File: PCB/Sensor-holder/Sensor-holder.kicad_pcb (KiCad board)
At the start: 2 copper layers, 35.1 x 22.9 mm, 25 parts, among them P1 CONN_01X05, Q1 IRLML6402, Q2 IRLML6402, Q3 IRLML6402, U1 DRV5013AD, U2 DRV5013AD, U3 DRV5013AD

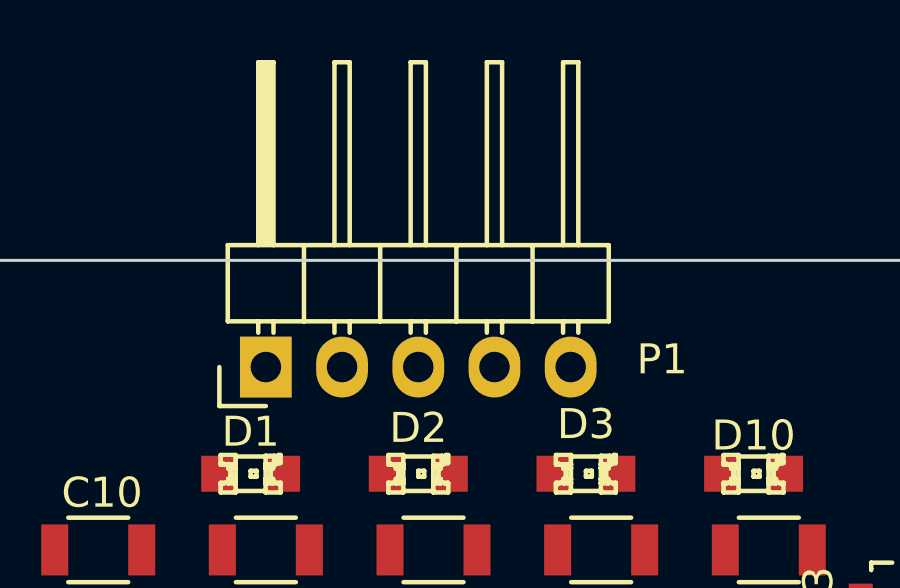
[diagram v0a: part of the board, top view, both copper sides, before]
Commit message: Design Regeln für die Leiterbahnen und Vias definiert. Einstellungen aus dem Teensy Projekt.
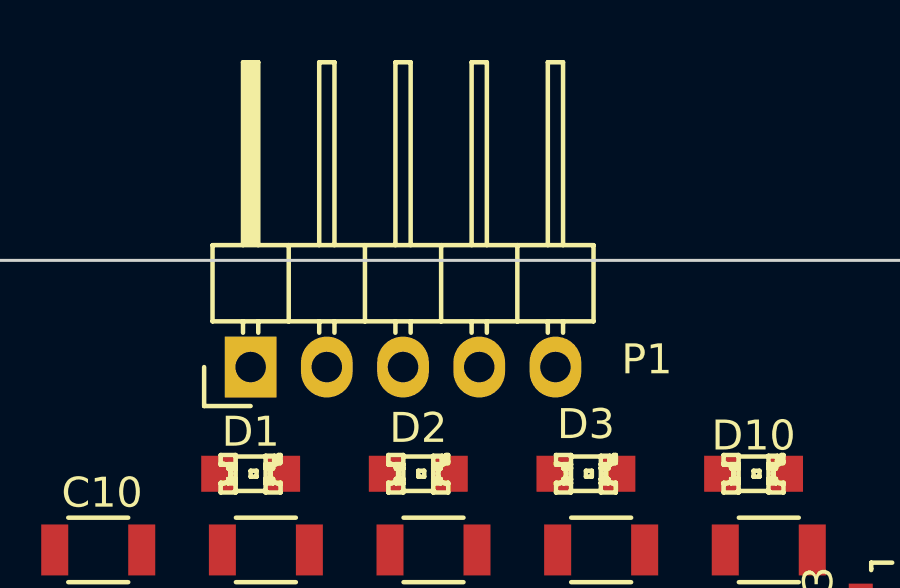
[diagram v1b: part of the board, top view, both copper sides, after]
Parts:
- moved P1 0.51 mm to (147.3, 106.2)
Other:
- net class 0,2 added: clearance 0.15, trace_width 0.2, via_dia 0.6, via_drill 0.3
- net class 0,25 added: clearance 0.15, trace_width 0.25, via_dia 0.6, via_drill 0.3
- net class 0,3 added: clearance 0.15, trace_width 0.3, via_dia 0.6, via_drill 0.3
- net class 0,4 added: clearance 0.15, trace_width 0.4, via_dia 0.6, via_drill 0.3
- net class 0,5 added: clearance 0.15, trace_width 0.5, via_dia 0.6, via_drill 0.3
- net class 0,7 added: clearance 0.15, trace_width 0.7, via_dia 0.6, via_drill 0.3
- net class 1,0 added: clearance 0.15, trace_width 1, via_dia 0.6, via_drill 0.3
- net class 1,5 added: clearance 0.15, trace_width 1.5, via_dia 0.6, via_drill 0.3
- net class 2,0 added: clearance 0.15, trace_width 2, via_dia 0.6, via_drill 0.3
- net class Default: clearance 0.254 -> 0.15; trace_width 0.254 -> 0.15; via_dia 0.889 -> 0.6; via_drill 0.635 -> 0.3
- rule trace_clearance: 0.254 -> 0.15
- rule trace_min: 0.254 -> 0.15
- rule via_min_drill: 0.508 -> 0.3
- rule via_min_size: 0.889 -> 0.6
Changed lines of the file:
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@@
     (links 47)
     (no_connects 47)
-    (area 136.601999 102.565999 171.754001 125.526001)
+    (area 120.295999 91.13 190.185544 187.044001)
     (thickness 1.6)
     (drawings 10)
@@
   )
   (setup
-    (last_trace_width 0.254)
-    (trace_clearance 0.254)
-    (zone_clearance 0.508)
+    (last_trace_width 0.15)
+    (user_trace_width 0.15)
+    (user_trace_width 0.2)
+    (user_trace_width 0.25)
+    (user_trace_width 0.3)
+    (user_trace_width 0.4)
+    (user_trace_width 0.5)
+    (user_trace_width 0.7)
+    (user_trace_width 1)
+    (user_trace_width 1.5)
+    (user_trace_width 2)
+    (trace_clearance 0.15)
+    (zone_clearance 0.15)
     (zone_45_only no)
-    (trace_min 0.254)
-    (segment_width 0.2)
+    (trace_min 0.15)
+    (segment_width 0.15)
     (edge_width 0.1)
-    (via_size 0.889)
-    (via_drill 0.635)
-    (via_min_size 0.889)
-    (via_min_drill 0.508)
-    (uvia_size 0.508)
-    (uvia_drill 0.127)
+    (via_size 0.6)
+    (via_drill 0.3)
+    (via_min_size 0.6)
+    (via_min_drill 0.3)
+    (user_via 0.6 0.3)
+    (user_via 0.7 0.4)
+    (user_via 0.8 0.5)
+    (user_via 0.9 0.6)
+    (user_via 1 0.7)
+    (user_via 1.1 0.8)
+    (user_via 1.2 0.9)
+    (user_via 1.3 1)
+    (uvia_size 0.6)
+    (uvia_drill 0.3)
     (uvias_allowed no)
-    (uvia_min_size 0.508)
-    (uvia_min_drill 0.127)
+    (uvia_min_size 0.6)
+    (uvia_min_drill 0.3)
     (pcb_text_width 0.3)
     (pcb_text_size 1.5 1.5)
@@
     (mod_text_size 1 1)
     (mod_text_width 0.15)
-    (pad_size 0.8001 0.8001)
-    (pad_drill 0)
+    (pad_size 1.4732 1.4732)
+    (pad_drill 0.9652)
     (pad_to_mask_clearance 0)
     (aux_axis_origin 0 0)
@@
   (net 12 "Net-(Q3-PadD)")
   (net_class Default "Dies ist die voreingestellte Netzklasse."
-    (clearance 0.254)
-    (trace_width 0.254)
-    (via_dia 0.889)
-    (via_drill 0.635)
-    (uvia_dia 0.508)
-    (uvia_drill 0.127)
+    (clearance 0.15)
+    (trace_width 0.15)
+    (via_dia 0.6)
+    (via_drill 0.3)
+    (uvia_dia 0.6)
+    (uvia_drill 0.3)
+  )
+  (net_class 0,2 ""
+    (clearance 0.15)
+    (trace_width 0.2)
+    (via_dia 0.6)
+    (via_drill 0.3)
+    (uvia_dia 0.6)
+    (uvia_drill 0.3)
+  )
+  (net_class 0,25 ""
+    (clearance 0.15)
+    (trace_width 0.25)
+    (via_dia 0.6)
+    (via_drill 0.3)
+    (uvia_dia 0.6)
+    (uvia_drill 0.3)
     (add_net /A)
     (add_net /B)
@@
     (add_net "Net-(Q2-PadD)")
     (add_net "Net-(Q3-PadD)")
+  )
+  (net_class 0,3 ""
+    (clearance 0.15)
+    (trace_width 0.3)
+    (via_dia 0.6)
+    (via_drill 0.3)
+    (uvia_dia 0.6)
+    (uvia_drill 0.3)
+  )
+  (net_class 0,4 ""
+    (clearance 0.15)
+    (trace_width 0.4)
+    (via_dia 0.6)
+    (via_drill 0.3)
+    (uvia_dia 0.6)
+    (uvia_drill 0.3)
+  )
+  (net_class 0,5 ""
+    (clearance 0.15)
+    (trace_width 0.5)
+    (via_dia 0.6)
+    (via_drill 0.3)
+    (uvia_dia 0.6)
+    (uvia_drill 0.3)
+  )
+  (net_class 0,7 ""
+    (clearance 0.15)
+    (trace_width 0.7)
+    (via_dia 0.6)
+    (via_drill 0.3)
+    (uvia_dia 0.6)
+    (uvia_drill 0.3)
+  )
+  (net_class 1,0 ""
+    (clearance 0.15)
+    (trace_width 1)
+    (via_dia 0.6)
+    (via_drill 0.3)
+    (uvia_dia 0.6)
+    (uvia_drill 0.3)
+  )
+  (net_class 1,5 ""
+    (clearance 0.15)
+    (trace_width 1.5)
+    (via_dia 0.6)
+    (via_drill 0.3)
+    (uvia_dia 0.6)
+    (uvia_drill 0.3)
+  )
+  (net_class 2,0 ""
+    (clearance 0.15)
+    (trace_width 2)
+    (via_dia 0.6)
+    (via_drill 0.3)
+    (uvia_dia 0.6)
+    (uvia_drill 0.3)
   )
   (module Resistors_SMD:R_1206 (layer F.Cu)
@@
   )
   (module Pin_Headers:Pin_Header_Angled_1x05 (layer F.Cu)
-    (at 147.828 106.172 90)
+    (at 147.32 106.172 90)
     (descr "Through hole pin header")
     (tags "pin header")

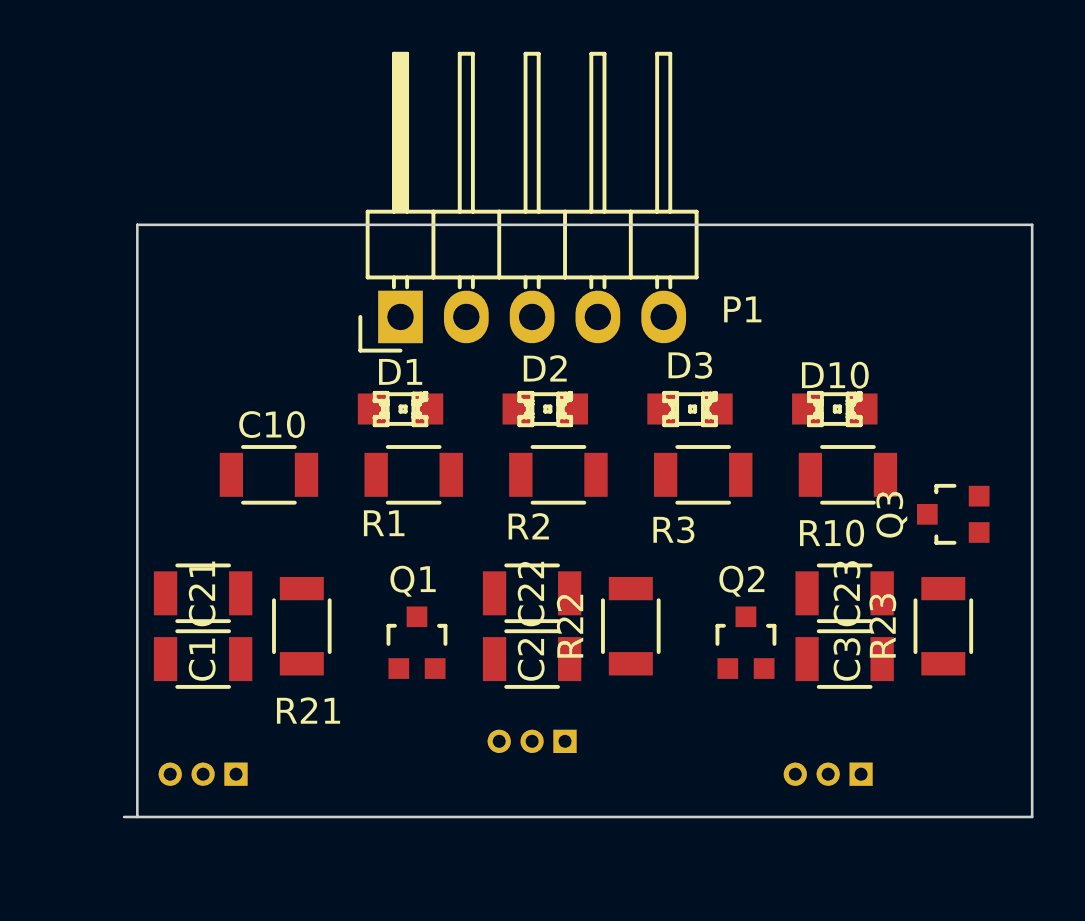
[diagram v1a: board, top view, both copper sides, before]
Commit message: Dip Switch eingearbeitet. Layout wird dadurch suboptimal.
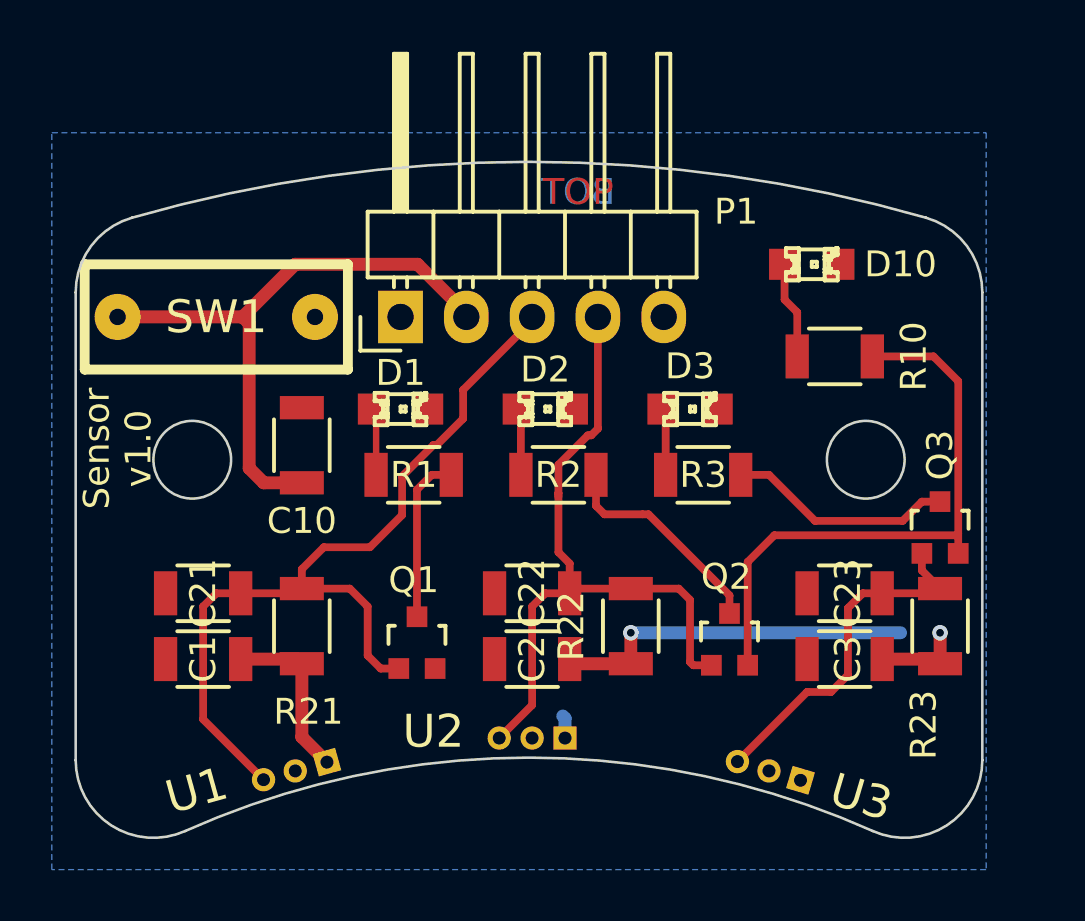
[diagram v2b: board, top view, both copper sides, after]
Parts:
- added SW1: LED, dips-s:DIPS-DS01, F.Cu at (140.2, 106.2)
- moved D10 5.66 mm to (163.2, 104.1)
- moved R10 4.60 mm to (164.1, 107.7)
- moved U1 3.56 mm to (143.3, 123.7), turned to 105.5 degrees
- moved U3 2.29 mm to (161.5, 123.7), turned to 73.5 degrees
- moved C10 1.71 mm to (143.5, 111.1), turned to 90 degrees
- moved Q3 0.72 mm to (168.1, 114.3), turned to 0 degrees
- moved Q2 0.65 mm to (160.0, 118.6)
- moved R23 0.13 mm to (168.1, 118.1)
- moved U2 0.13 mm to (152.4, 122.4)
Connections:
- Q1 pad S: /Vcc -> Net-(Q1-PadS)
- Q2 pad S: /Vcc -> Net-(Q1-PadS)
- Q3 pad S: /Vcc -> Net-(Q1-PadS)
- R10 pad 1: /Vcc -> Net-(Q1-PadS)
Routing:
- net /Vcc: track 0.00 -> 48.8 mm, vias 0 -> 2
- net /A: track 0.00 -> 33.2 mm
- net /B: track 0.00 -> 27.1 mm
- net Net-(Q1-PadS): track 0.00 -> 22.9 mm
- net /C: track 0.00 -> 13.9 mm
- net Net-(Q3-PadD): track 0.00 -> 8.74 mm
- net Net-(Q2-PadD): track 0.00 -> 8.48 mm
- net Net-(Q1-PadD): track 0.00 -> 6.47 mm
- net Net-(D10-Pad1): track 0.00 -> 3.76 mm
- net Net-(D1-Pad1): track 0.00 -> 2.74 mm
- net Net-(D3-Pad1): track 0.00 -> 2.58 mm
- net Net-(D2-Pad1): track 0.00 -> 2.58 mm
- added copper zone on B.Cu, net /Vcc
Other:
- board size 35.1 x 22.9 mm -> 35 x 26.1 mm
- board text added: "BOT"
- board text added: "Sensor v1.0"
- board text added: "TOP"
